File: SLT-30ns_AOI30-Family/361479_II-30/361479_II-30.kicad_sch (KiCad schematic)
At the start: 9 parts, among them T1 ABA, T2 ABA, U1 12-Pin_SLx_Can

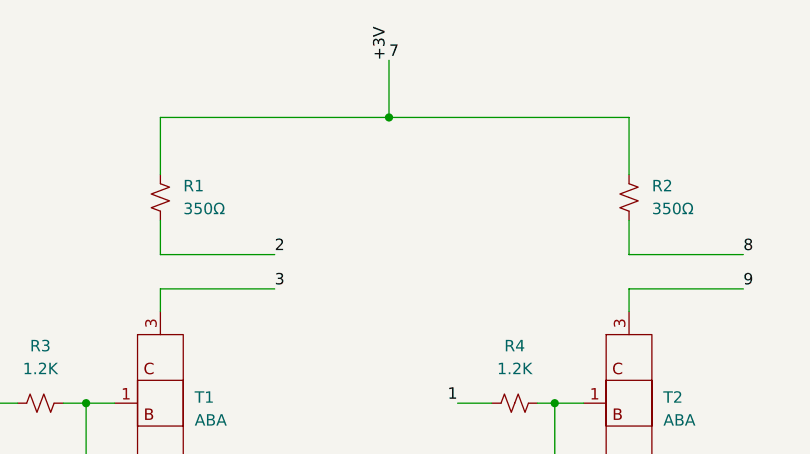
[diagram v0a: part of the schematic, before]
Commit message: Update schematic pdfs
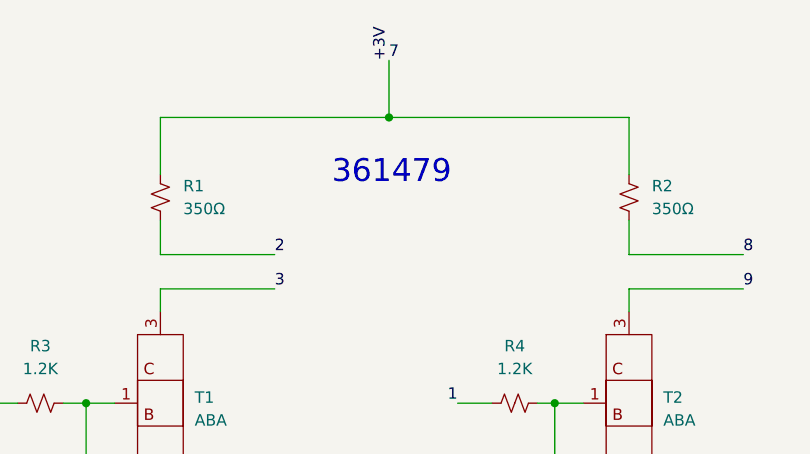
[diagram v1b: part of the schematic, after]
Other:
- note added: "361479"
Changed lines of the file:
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@@
     (stroke (width 0) (type default) (color 0 0 0 0))
+  )
+  (text "361479" (at 109.22 80.01 0)
+    (effects (font (size 2.54 2.54)) (justify left bottom))
   )
   (label "8" (at 154.94 87.63 0)
